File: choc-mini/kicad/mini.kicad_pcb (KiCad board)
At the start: 2 copper layers, 126.3 x 89.3 mm, 22 parts

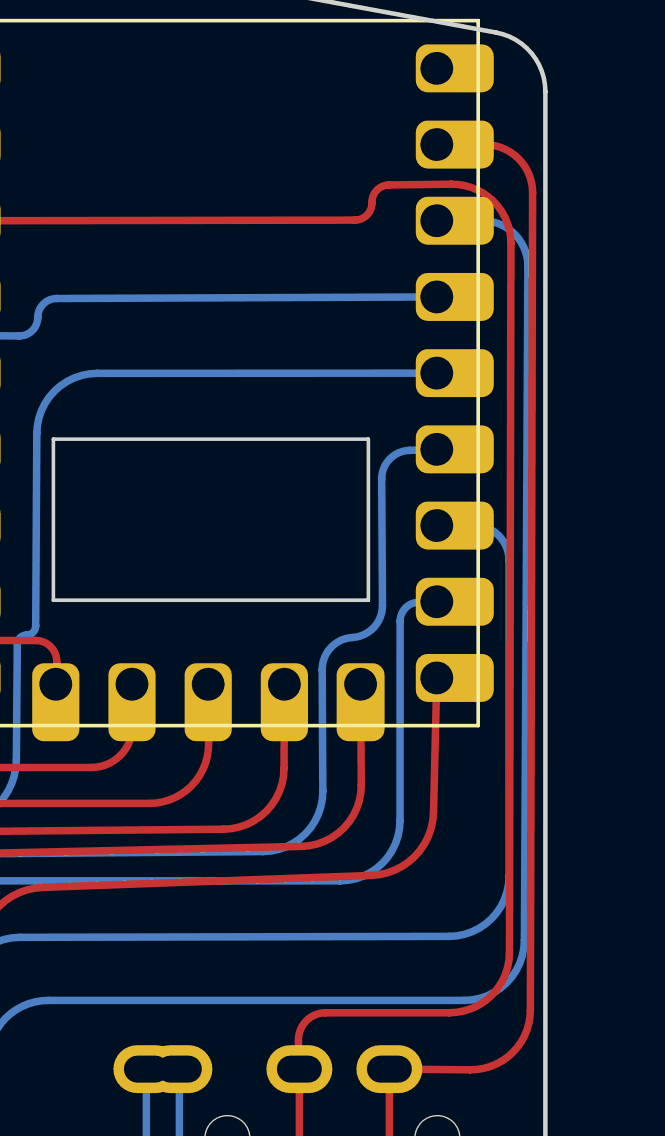
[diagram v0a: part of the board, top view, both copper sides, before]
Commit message: add more clearance to 3.3v route
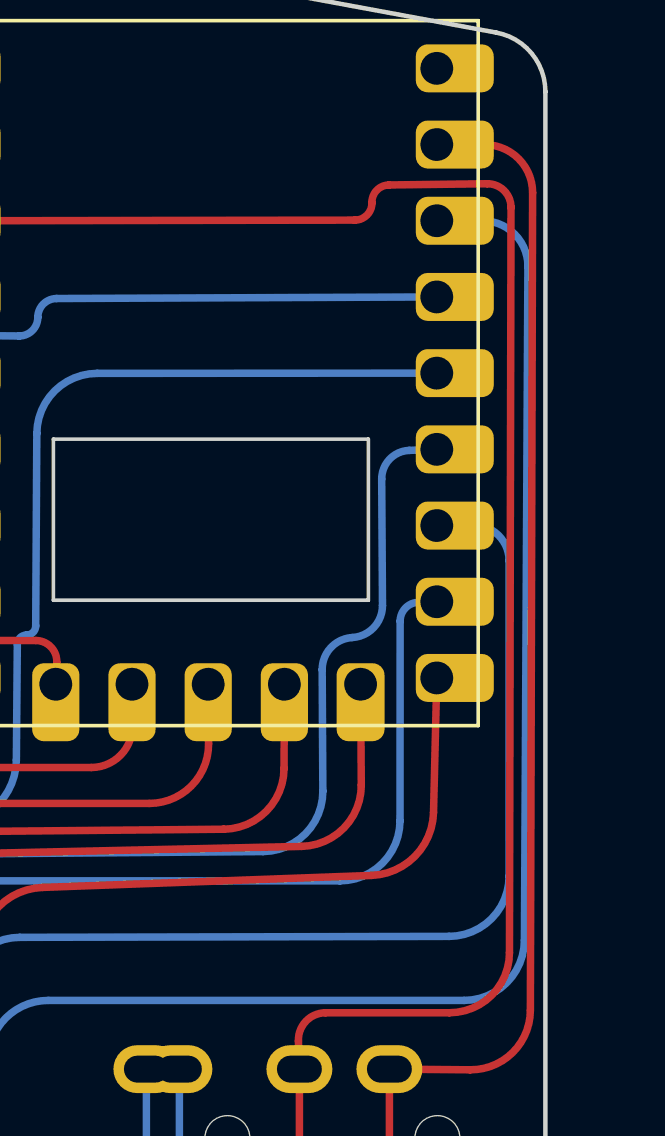
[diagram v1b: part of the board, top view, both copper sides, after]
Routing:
- net P3V3: track 57.2 -> 57.8 mm
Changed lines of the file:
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@@
   (segment (start 200.944114 81.55447) (end 196.822178 81.55447) (width 0.25) (layer "F.Cu") (net 20))
   (segment (start 197.795889 55.133326) (end 185.2866 55.1538) (width 0.25) (layer "F.Cu") (net 20))
-  (segment (start 202.998253 55.905088) (end 202.949129 79.553615) (width 0.25) (layer "F.Cu") (net 20))
-  (segment (start 201.008544 53.935705) (end 198.933182 53.961327) (width 0.25) (layer "F.Cu") (net 20))
+  (segment (start 203.000745 54.705592) (end 202.949129 79.553615) (width 0.25) (layer "F.Cu") (net 20))
+  (segment (start 202.20795 53.920897) (end 198.933182 53.961327) (width 0.25) (layer "F.Cu") (net 20))
   (segment (start 195.914279 82.494135) (end 195.9466 83.4338) (width 0.25) (layer "F.Cu") (net 20))
   (arc (start 196.822178 81.55447) (mid 196.168869 81.831682) (end 195.914279 82.494135) (width 0.25) (layer "F.Cu") (net 20))
   (arc (start 198.364558 54.550443) (mid 198.202774 54.961447) (end 197.795889 55.133326) (width 0.25) (layer "F.Cu") (net 20))
   (arc (start 198.933182 53.961327) (mid 198.525935 54.137226) (end 198.364558 54.550443) (width 0.25) (layer "F.Cu") (net 20))
-  (arc (start 202.998253 55.905088) (mid 202.415437 54.504105) (end 201.008544 53.935705) (width 0.25) (layer "F.Cu") (net 20))
+  (arc (start 203.000745 54.705592) (mid 202.768523 54.147374) (end 202.20795 53.920897) (width 0.25) (layer "F.Cu") (net 20))
   (arc (start 202.949129 79.553615) (mid 202.360403 80.968685) (end 200.944114 81.55447) (width 0.25) (layer "F.Cu") (net 20))
   (segment (start 203.72073 54.219652) (end 203.645995 81.474048) (width 0.25) (layer "F.Cu") (net 21))
